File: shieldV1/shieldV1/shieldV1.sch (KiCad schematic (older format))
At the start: 6 parts, among them J1 Conn_02x19_Odd_Even, J2 Conn_02x19_Odd_Even, J3 Conn_01x04_Female, J4 Conn_01x04_Female, J5 Conn_01x03_Female

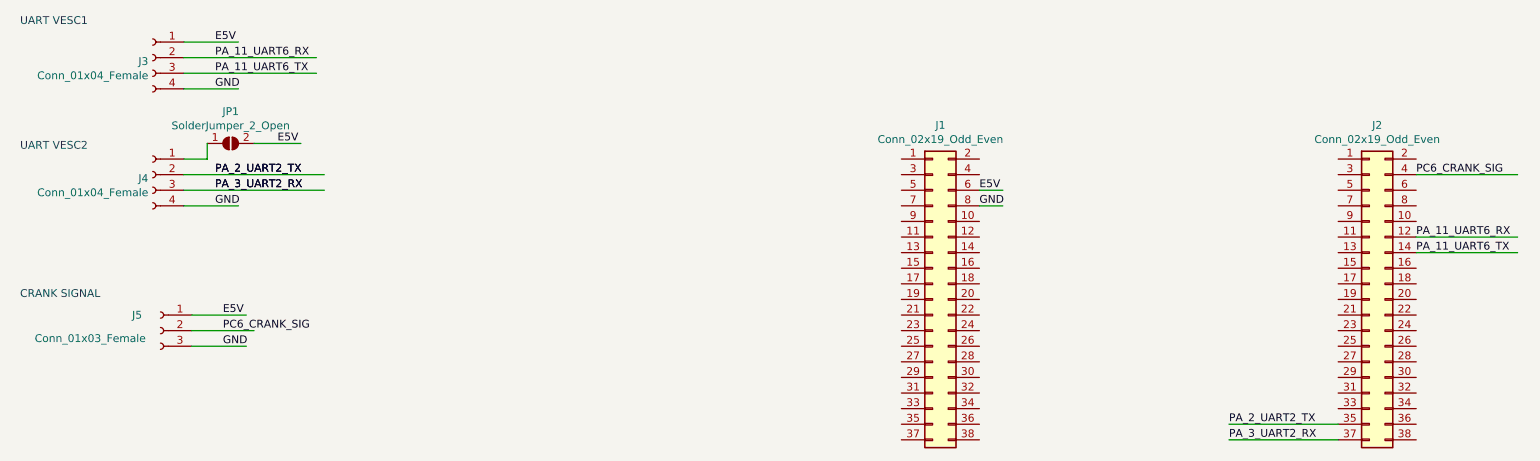
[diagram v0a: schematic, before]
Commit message: Modify GND symbol and crank signal wiring
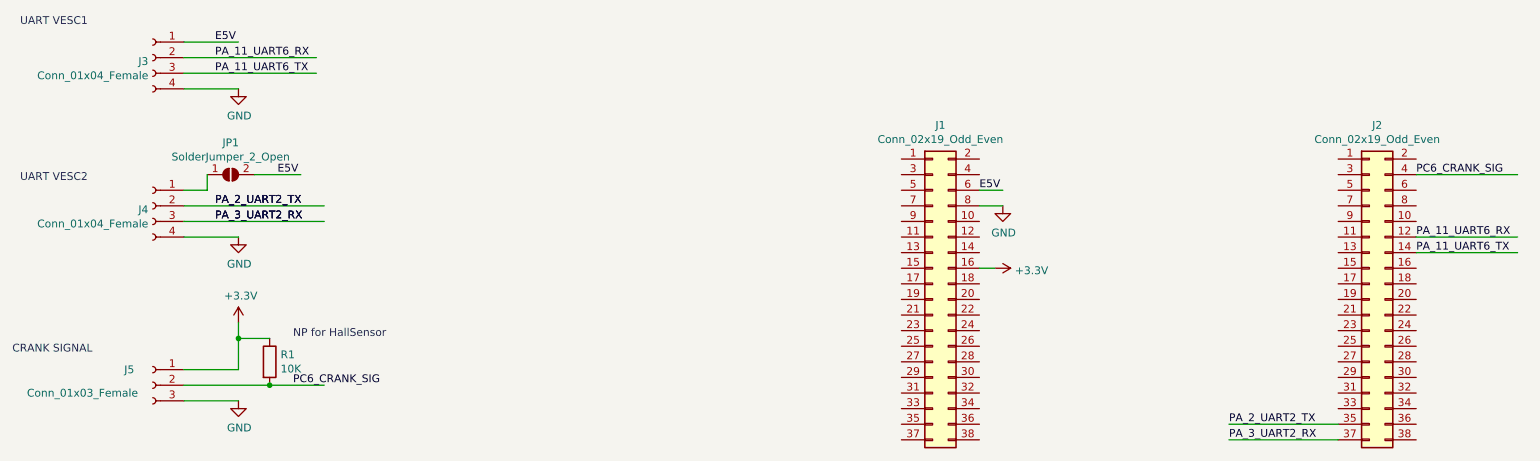
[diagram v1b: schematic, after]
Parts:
- added R1: 10K, Resistor_SMD:R_0603_1608Metric, symbol Device:R
- JP1: footprint (none) -> Jumper:SolderJumper-2_P1.3mm_Open_RoundedPad1.0x1.5mm
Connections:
- net labels added: +3.3V
- wire segments 20 -> 25
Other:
- note added: "NP for HallSensor"
- moved on the sheet: J4, J5, JP1
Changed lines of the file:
@@
 encoding utf-8
 Sheet 1 1
-Title ""
+Title "Nucleo Shield"
 Date ""
-Rev ""
-Comp ""
+Rev "V1"
+Comp "Coilchain"
 Comment1 ""
 Comment2 ""
@@
 L Connector:Conn_01x04_Female J4
 U 1 1 601B0759
-P 1700 2000
-F 0 "J4" H 1728 1976 50  0000 L CNN
-F 1 "Conn_01x04_Female" H 1728 1885 50  0000 L CNN
-F 2 "Connector_JST:JST_GH_BM04B-GHS-TBT_1x04-1MP_P1.25mm_Vertical" H 1700 2000 50  0001 C CNN
-F 3 "~" H 1700 2000 50  0001 C CNN
-	1    1700 2000
+P 1700 2200
+F 0 "J4" H 1728 2176 50  0000 L CNN
+F 1 "Conn_01x04_Female" H 1728 2085 50  0000 L CNN
+F 2 "Connector_JST:JST_GH_BM04B-GHS-TBT_1x04-1MP_P1.25mm_Vertical" H 1700 2200 50  0001 C CNN
+F 3 "~" H 1700 2200 50  0001 C CNN
+	1    1700 2200
 	-1   0    0    -1
 $EndComp
 Text Label 7000 2100 0    50   ~ 0
 E5V
-Text Label 7000 2200 0    50   ~ 0
-GND
 Text Label 9800 2500 0    50   ~ 0
 PA_11_UART6_TX
@@
 Text Label 2100 1150 0    50   ~ 0
 E5V
-Text Label 2500 1800 0    50   ~ 0
+Text Label 2500 2000 0    50   ~ 0
 E5V
-Text Label 2100 2200 0    50   ~ 0
-GND
-Text Label 2100 1450 0    50   ~ 0
-GND
-Text Label 2100 2100 0    50   ~ 0
+Text Label 2100 2300 0    50   ~ 0
 PA_3_UART2_RX
-Text Label 2100 2000 0    50   ~ 0
+Text Label 2100 2200 0    50   ~ 0
 PA_2_UART2_TX
-Text Label 2100 2100 0    50   ~ 0
+Text Label 2100 2300 0    50   ~ 0
 PA_3_UART2_RX
-Text Label 2100 2000 0    50   ~ 0
+Text Label 2100 2200 0    50   ~ 0
 PA_2_UART2_TX
 Text Label 2100 1350 0    50   ~ 0
@@
 L Jumper:SolderJumper_2_Open JP1
 U 1 1 601C8306
-P 2200 1800
-F 0 "JP1" H 2200 2005 50  0000 C CNN
-F 1 "SolderJumper_2_Open" H 2200 1914 50  0000 C CNN
-F 2 "" H 2200 1800 50  0001 C CNN
-F 3 "~" H 2200 1800 50  0001 C CNN
-	1    2200 1800
+P 2200 2000
+F 0 "JP1" H 2200 2205 50  0000 C CNN
+F 1 "SolderJumper_2_Open" H 2200 2114 50  0000 C CNN
+F 2 "Jumper:SolderJumper-2_P1.3mm_Open_RoundedPad1.0x1.5mm" H 2200 2000 50  0001 C CNN
+F 3 "~" H 2200 2000 50  0001 C CNN
+	1    2200 2000
 	1    0    0    -1
 $EndComp
 Wire Wire Line
-	1900 1900 2050 1900
+	1900 2100 2050 2100
 Wire Wire Line
-	2050 1900 2050 1800
+	2050 2100 2050 2000
 Wire Wire Line
-	2350 1800 2650 1800
+	2350 2000 2650 2000
 Wire Wire Line
-	1900 2000 2800 2000
+	1900 2200 2800 2200
 Wire Wire Line
-	1900 2100 2800 2100
+	1900 2300 2800 2300
 Wire Wire Line
-	1900 2200 2250 2200
+	1900 2400 2250 2400
 $Comp
 L Connector:Conn_01x03_Female J5
 U 1 1 601CB229
-P 1750 3000
-F 0 "J5" H 1900 3100 50  0000 C CNN
-F 1 "Conn_01x03_Female" H 2200 2950 50  0000 C CNN
-F 2 "Connector_JST:JST_GH_BM03B-GHS-TBT_1x03-1MP_P1.25mm_Vertical" H 1750 3000 50  0001 C CNN
-F 3 "~" H 1750 3000 50  0001 C CNN
-	1    1750 3000
+P 1700 3350
+F 0 "J5" H 1850 3450 50  0000 C CNN
+F 1 "Conn_01x03_Female" H 2150 3300 50  0000 C CNN
+F 2 "Connector_JST:JST_GH_BM03B-GHS-TBT_1x03-1MP_P1.25mm_Vertical" H 1700 3350 50  0001 C CNN
+F 3 "~" H 1700 3350 50  0001 C CNN
+	1    1700 3350
 	-1   0    0    -1
 $EndComp
-Text Label 2150 2900 0    50   ~ 0
-E5V
-Text Label 2150 3100 0    50   ~ 0
-GND
 Wire Wire Line
-	1950 3100 2300 3100
+	1900 3450 2250 3450
 Wire Wire Line
-	1950 2900 2300 2900
-Text Label 2150 3000 0    50   ~ 0
+	1900 3250 2250 3250
+Text Label 2600 3350 0    50   ~ 0
 PC6_CRANK_SIG
-Wire Wire Line
-	1950 3000 2350 3000
 Text Notes 850  1050 0    50   ~ 0
 UART VESC1
-Text Notes 850  1850 0    50   ~ 0
+Text Notes 850  2050 0    50   ~ 0
 UART VESC2
-Text Notes 850  2800 0    50   ~ 0
+Text Notes 800  3150 0    50   ~ 0
 CRANK SIGNAL
 Text Label 9800 2000 0    50   ~ 0
@@
 Wire Wire Line
 	9800 2000 10450 2000
+$Comp
+L power:+3.3V #PWR02
+U 1 1 601D59A0
+P 7100 2600
+F 0 "#PWR02" H 7100 2450 50  0001 C CNN
+F 1 "+3.3V" V 7115 2728 50  0000 L CNN
+F 2 "" H 7100 2600 50  0001 C CNN
+F 3 "" H 7100 2600 50  0001 C CNN
+	1    7100 2600
+	0    1    1    0
+$EndComp
+Wire Wire Line
+	7100 2600 7000 2600
+$Comp
+L power:+3.3V #PWR01
+U 1 1 601DB67C
+P 2250 2950
+F 0 "#PWR01" H 2250 2800 50  0001 C CNN
+F 1 "+3.3V" H 2265 3123 50  0000 C CNN
+F 2 "" H 2250 2950 50  0001 C CNN
+F 3 "" H 2250 2950 50  0001 C CNN
+	1    2250 2950
+	1    0    0    -1
+$EndComp
+$Comp
+L Device:R R1
+U 1 1 601DDB79
+P 2450 3200
+F 0 "R1" H 2520 3246 50  0000 L CNN
+F 1 "10K" H 2520 3155 50  0000 L CNN
+F 2 "Resistor_SMD:R_0603_1608Metric" V 2380 3200 50  0001 C CNN
+F 3 "~" H 2450 3200 50  0001 C CNN
+	1    2450 3200
+	1    0    0    -1
+$EndComp
+Wire Wire Line
+	1900 3350 2450 3350
+Connection ~ 2450 3350
+Wire Wire Line
+	2450 3350 2800 3350
+Wire Wire Line
+	2250 3250 2250 3050
+Wire Wire Line
+	2450 3050 2250 3050
+Connection ~ 2250 3050
+Wire Wire Line
+	2250 3050 2250 2950
+Text Notes 2600 3050 0    50   ~ 0
+NP for HallSensor
+$Comp
+L power:GND #PWR?
+U 1 1 601E0CC8
+P 7150 2200
+F 0 "#PWR?" H 7150 1950 50  0001 C CNN
+F 1 "GND" H 7155 2027 50  0000 C CNN
+F 2 "" H 7150 2200 50  0001 C CNN
+F 3 "" H 7150 2200 50  0001 C CNN
+	1    7150 2200
+	1    0    0    -1
+$EndComp
+$Comp
+L power:GND #PWR?
+U 1 1 601E12E4
+P 2250 3450
+F 0 "#PWR?" H 2250 3200 50  0001 C CNN
+F 1 "GND" H 2255 3277 50  0000 C CNN
+F 2 "" H 2250 3450 50  0001 C CNN
+F 3 "" H 2250 3450 50  0001 C CNN
+	1    2250 3450
+	1    0    0    -1
+$EndComp
+$Comp
+L power:GND #PWR?
+U 1 1 601E1BD2
+P 2250 2400
+F 0 "#PWR?" H 2250 2150 50  0001 C CNN
+F 1 "GND" H 2255 2227 50  0000 C CNN
+F 2 "" H 2250 2400 50  0001 C CNN
+F 3 "" H 2250 2400 50  0001 C CNN
+	1    2250 2400
+	1    0    0    -1
+$EndComp
+$Comp
+L power:GND #PWR?
+U 1 1 601E1FA6
+P 2250 1450
+F 0 "#PWR?" H 2250 1200 50  0001 C CNN
+F 1 "GND" H 2255 1277 50  0000 C CNN
+F 2 "" H 2250 1450 50  0001 C CNN
+F 3 "" H 2250 1450 50  0001 C CNN
+	1    2250 1450
+	1    0    0    -1
+$EndComp
 $EndSCHEMATC

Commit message: Chage JST to Horizontal
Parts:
- J3, J4: footprint Connector_JST:JST_GH_BM04B-GHS-TBT_1x04-1MP_P1.25mm_Vertical -> Connector_JST:JST_GH_SM04B-GHS-TB_1x04-1MP_P1.25mm_Horizontal
- J5: footprint Connector_JST:JST_GH_BM03B-GHS-TBT_1x03-1MP_P1.25mm_Vertical -> Connector_JST:JST_GH_SM03B-GHS-TB_1x03-1MP_P1.25mm_Horizontal
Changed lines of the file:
@@
 F 0 "J3" H 1728 1226 50  0000 L CNN
 F 1 "Conn_01x04_Female" H 1728 1135 50  0000 L CNN
-F 2 "Connector_JST:JST_GH_BM04B-GHS-TBT_1x04-1MP_P1.25mm_Vertical" H 1700 1250 50  0001 C CNN
+F 2 "Connector_JST:JST_GH_SM04B-GHS-TB_1x04-1MP_P1.25mm_Horizontal" H 1700 1250 50  0001 C CNN
 F 3 "~" H 1700 1250 50  0001 C CNN
 	1    1700 1250
@@
 F 0 "J4" H 1728 2176 50  0000 L CNN
 F 1 "Conn_01x04_Female" H 1728 2085 50  0000 L CNN
-F 2 "Connector_JST:JST_GH_BM04B-GHS-TBT_1x04-1MP_P1.25mm_Vertical" H 1700 2200 50  0001 C CNN
+F 2 "Connector_JST:JST_GH_SM04B-GHS-TB_1x04-1MP_P1.25mm_Horizontal" H 1700 2200 50  0001 C CNN
 F 3 "~" H 1700 2200 50  0001 C CNN
 	1    1700 2200
@@
 F 0 "J5" H 1850 3450 50  0000 C CNN
 F 1 "Conn_01x03_Female" H 2150 3300 50  0000 C CNN
-F 2 "Connector_JST:JST_GH_BM03B-GHS-TBT_1x03-1MP_P1.25mm_Vertical" H 1700 3350 50  0001 C CNN
+F 2 "Connector_JST:JST_GH_SM03B-GHS-TB_1x03-1MP_P1.25mm_Horizontal" H 1700 3350 50  0001 C CNN
 F 3 "~" H 1700 3350 50  0001 C CNN
 	1    1700 3350
@@
 NP for HallSensor
 $Comp
-L power:GND #PWR?
+L power:GND #PWR0101
 U 1 1 601E0CC8
 P 7150 2200
-F 0 "#PWR?" H 7150 1950 50  0001 C CNN
+F 0 "#PWR0101" H 7150 1950 50  0001 C CNN
 F 1 "GND" H 7155 2027 50  0000 C CNN
 F 2 "" H 7150 2200 50  0001 C CNN
@@
 $EndComp
 $Comp
-L power:GND #PWR?
+L power:GND #PWR0102
 U 1 1 601E12E4
 P 2250 3450
-F 0 "#PWR?" H 2250 3200 50  0001 C CNN
+F 0 "#PWR0102" H 2250 3200 50  0001 C CNN
 F 1 "GND" H 2255 3277 50  0000 C CNN
 F 2 "" H 2250 3450 50  0001 C CNN
@@
 $EndComp
 $Comp
-L power:GND #PWR?
+L power:GND #PWR0103
 U 1 1 601E1BD2
 P 2250 2400
-F 0 "#PWR?" H 2250 2150 50  0001 C CNN
+F 0 "#PWR0103" H 2250 2150 50  0001 C CNN
 F 1 "GND" H 2255 2227 50  0000 C CNN
 F 2 "" H 2250 2400 50  0001 C CNN
@@
 $EndComp
 $Comp
-L power:GND #PWR?
+L power:GND #PWR0104
 U 1 1 601E1FA6
 P 2250 1450
-F 0 "#PWR?" H 2250 1200 50  0001 C CNN
+F 0 "#PWR0104" H 2250 1200 50  0001 C CNN
 F 1 "GND" H 2255 1277 50  0000 C CNN
 F 2 "" H 2250 1450 50  0001 C CNN
